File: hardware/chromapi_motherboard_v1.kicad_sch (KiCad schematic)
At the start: 9 parts

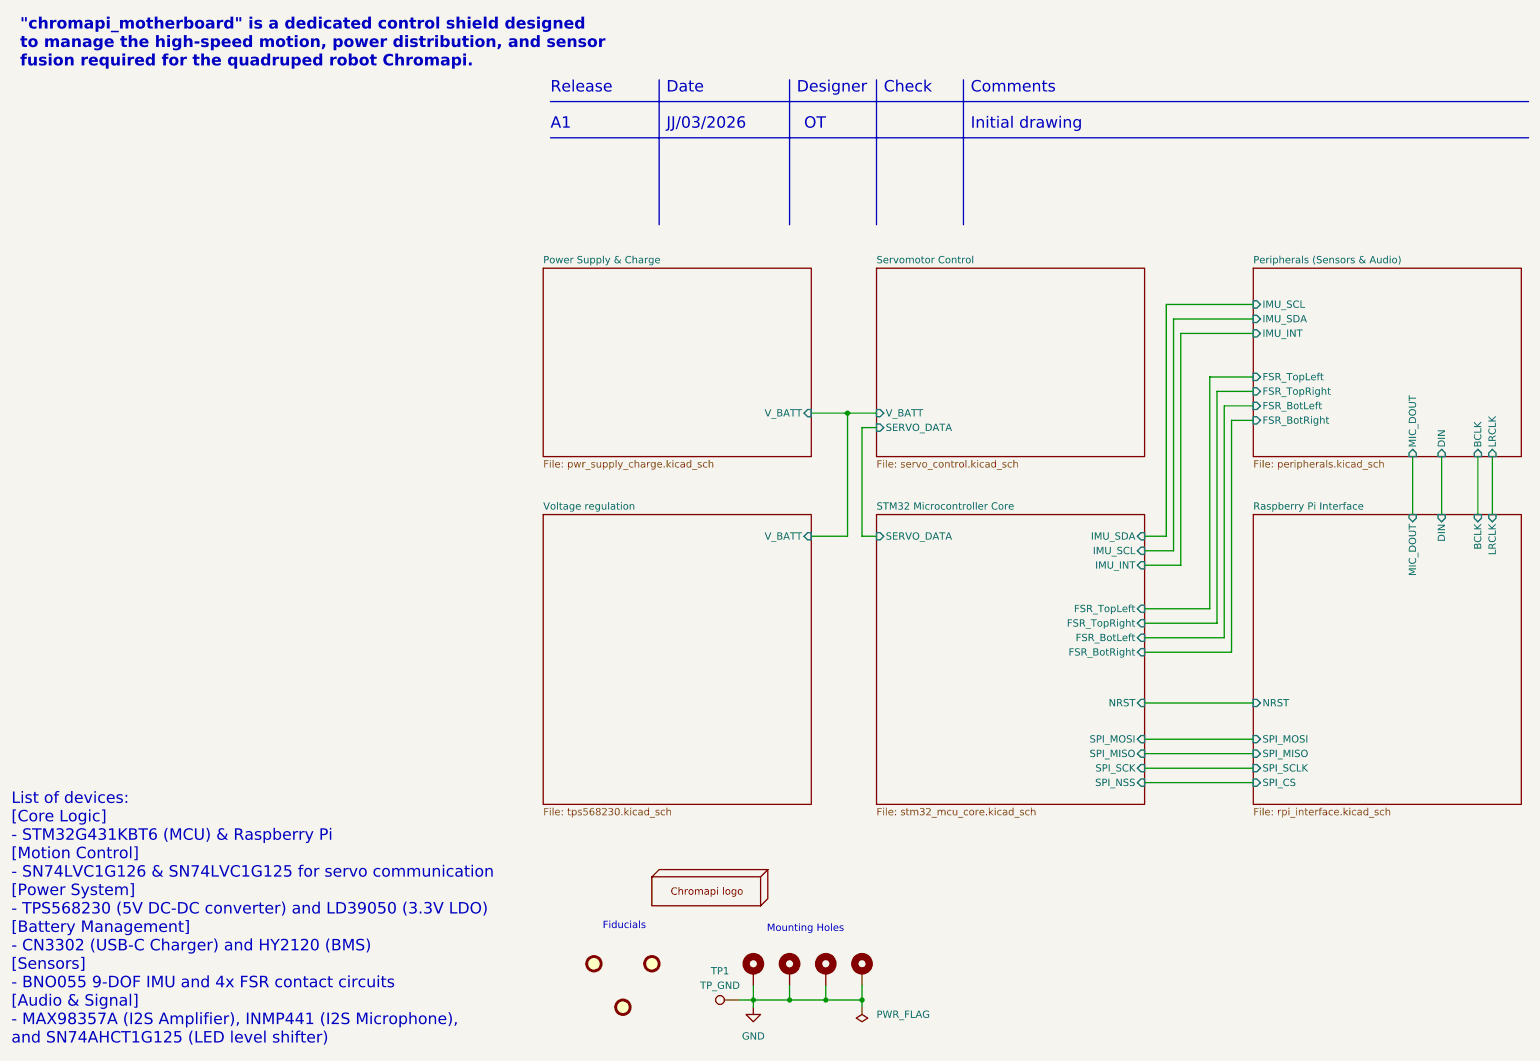
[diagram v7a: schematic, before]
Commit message: IMU modification and Power monitor addition
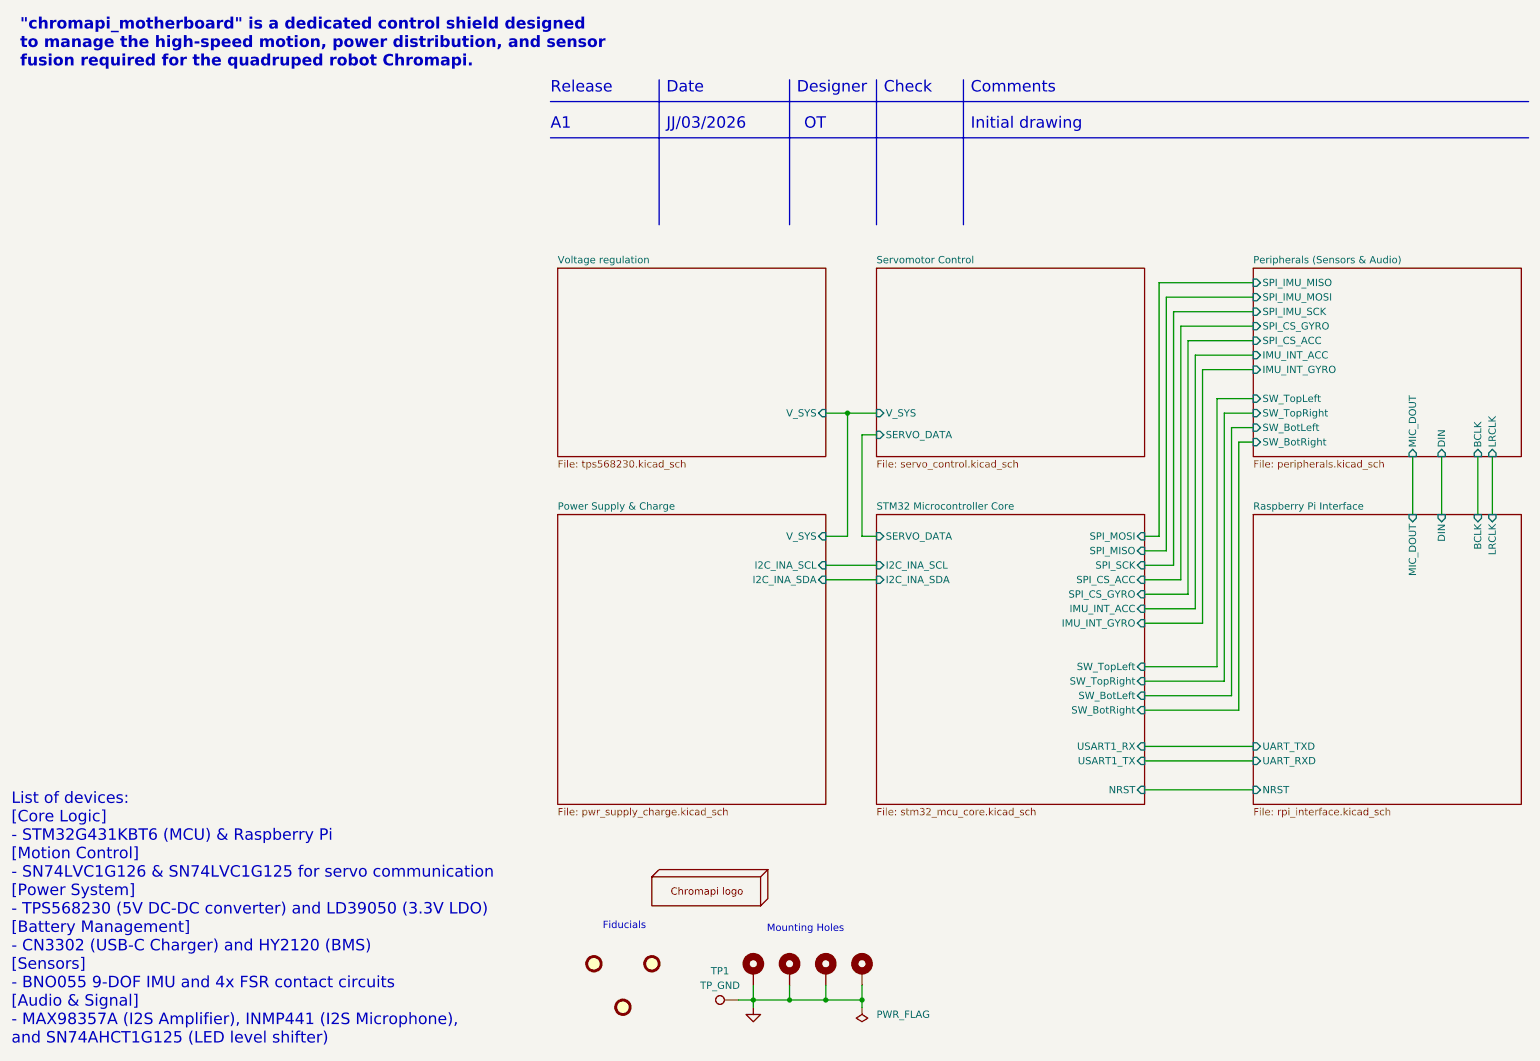
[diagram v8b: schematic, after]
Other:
- sheet Peripherals (Sensors & Audio) ports: added IMU_INT_ACC, IMU_INT_GYRO, SPI_CS_ACC, SPI_CS_GYRO, SPI_IMU_MISO, SPI_IMU_MOSI, SPI_IMU_SCK, SW_BotLeft, SW_BotRight, SW_TopLeft, SW_TopRight; removed FSR_BotLeft, FSR_BotRight, FSR_TopLeft, FSR_TopRight, IMU_INT, IMU_SCL, IMU_SDA
- sheet Power Supply & Charge ports: added I2C_INA_SCL, I2C_INA_SDA, V_SYS; removed V_BATT
- sheet Raspberry Pi Interface ports: added UART_RXD, UART_TXD; removed SPI_CS, SPI_MISO, SPI_MOSI, SPI_SCLK
- sheet STM32 Microcontroller Core ports: added I2C_INA_SCL, I2C_INA_SDA, IMU_INT_ACC, IMU_INT_GYRO, SPI_CS_ACC, SPI_CS_GYRO, SW_BotLeft, SW_BotRight, SW_TopLeft, SW_TopRight, USART1_RX, USART1_TX; removed FSR_BotLeft, FSR_BotRight, FSR_TopLeft, FSR_TopRight, IMU_INT, IMU_SCL, IMU_SDA, SPI_NSS
- sheet Servomotor Control ports: added V_SYS; removed V_BATT
- sheet Voltage regulation ports: added V_SYS; removed V_BATT
